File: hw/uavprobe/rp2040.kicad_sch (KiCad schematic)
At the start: 44 parts, among them IC1 UCLAMP3306P.TCT, SW1 Boot, U1 W25Q16JVSS, U2 NCP1117-5.0_SOT223, U3 RP2040, U4 TJA1051T-3, U5 TJA1051T-3, Y1 ABLS-12.000MHZ-B4-T

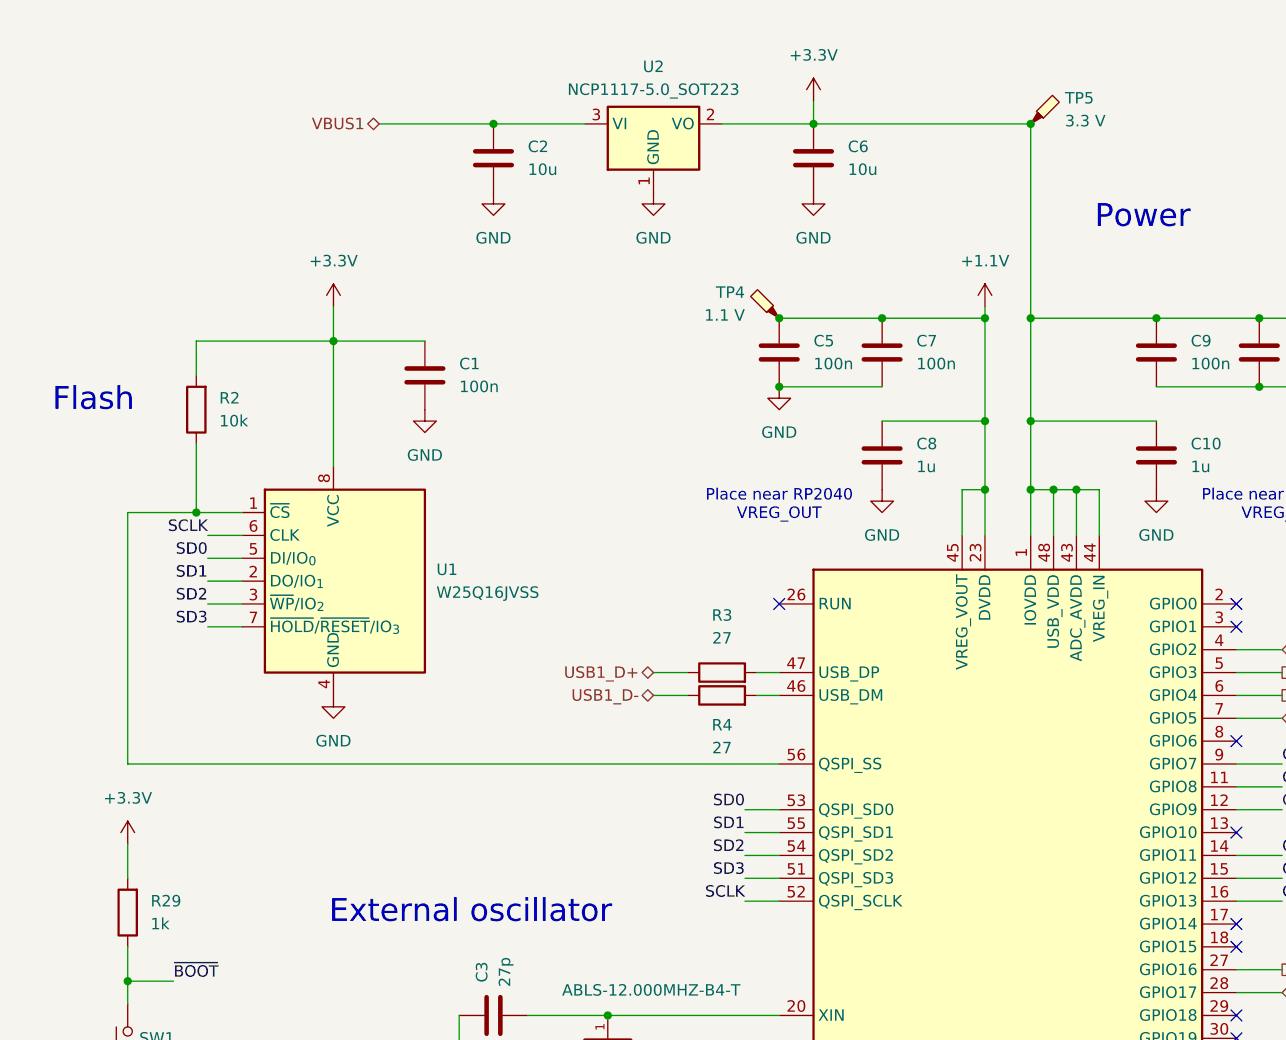
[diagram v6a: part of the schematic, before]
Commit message: Training layout
Lessons were learned, let's restart.
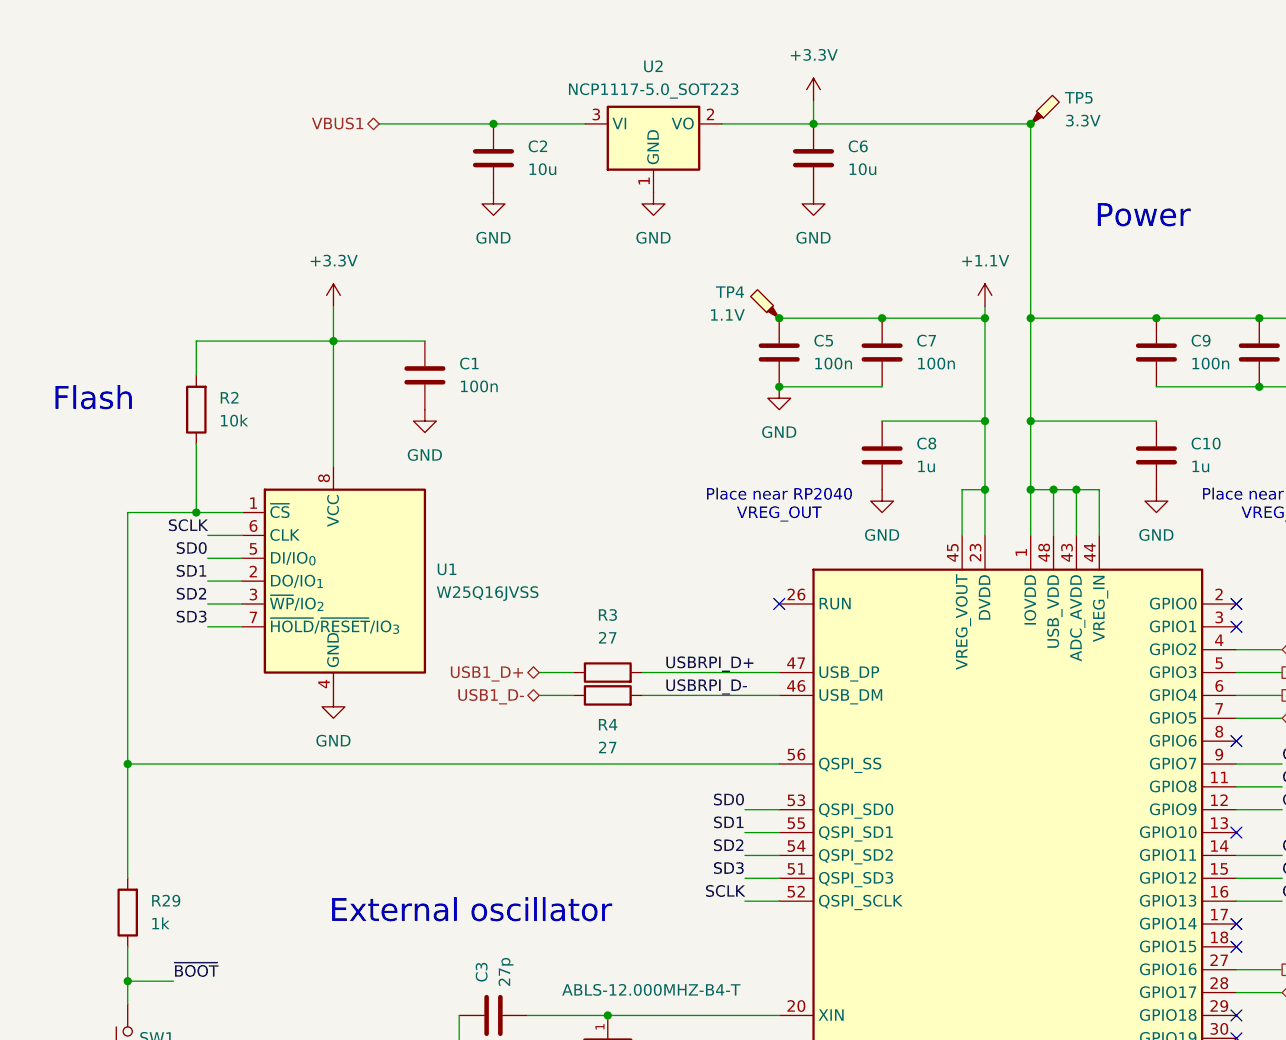
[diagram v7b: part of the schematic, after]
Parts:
- R3, R4: footprint Resistor_SMD:R_0402_1005Metric -> Resistor_SMD:R_0603_1608Metric
- TP4: value 1.1 V -> 1.1V
- TP5: value 3.3 V -> 3.3V
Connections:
- net +3.3V: no longer R29.2
- net USBRPI_D+: now reaches R3.2, U3.47 (USB_DP)
- net USBRPI_D-: now reaches R4.2, U3.46 (USB_DM)
- net at R2.1, U1.1 (~{CS}), U3.56 (QSPI_SS): now also R29.2
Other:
- moved on the sheet: R3, R4
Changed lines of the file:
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@@
 	)
 	(junction
+		(at 25.4 99.06)
+		(diameter 0)
+		(color 0 0 0 0)
+	)
+	(junction
 		(at 173.99 57.15)
 		(diameter 0)
@@
 	(wire
 		(pts
-			(xy 25.4 111.76) (xy 25.4 107.95)
-		)
-		(stroke
-			(width 0)
-			(type default)
-		)
-	)
-	(wire
-		(pts
-			(xy 95.25 88.9) (xy 97.79 88.9)
+			(xy 82.55 88.9) (xy 97.79 88.9)
 		)
 		(stroke
@@
 	(wire
 		(pts
-			(xy 95.25 91.44) (xy 97.79 91.44)
+			(xy 82.55 91.44) (xy 97.79 91.44)
 		)
 		(stroke
@@
 	(wire
 		(pts
+			(xy 25.4 111.76) (xy 25.4 99.06)
+		)
+		(stroke
+			(width 0)
+			(type default)
+		)
+	)
+	(wire
+		(pts
 			(xy 246.38 139.7) (xy 251.46 139.7)
 		)
@@
 	(wire
 		(pts
-			(xy 83.82 88.9) (xy 87.63 88.9)
+			(xy 71.12 88.9) (xy 74.93 88.9)
 		)
 		(stroke
@@
 	(wire
 		(pts
-			(xy 83.82 91.44) (xy 87.63 91.44)
+			(xy 71.12 91.44) (xy 74.93 91.44)
 		)
 		(stroke
@@
 		)
 	)
+	(label "USBRPI_D-"
+		(at 85.09 91.44 0)
+		(effects
+			(font
+				(size 1.27 1.27)
+			)
+			(justify left bottom)
+		)
+	)
+	(label "USBRPI_D+"
+		(at 85.09 88.9 0)
+		(effects
+			(font
+				(size 1.27 1.27)
+			)
+			(justify left bottom)
+		)
+	)
 	(label "SCLK"
 		(at 34.29 73.66 180)
@@
 	(hierarchical_label "USB1_D+"
 		(shape bidirectional)
-		(at 83.82 88.9 180)
+		(at 71.12 88.9 180)
 		(effects
 			(font
@@
 	(hierarchical_label "USB1_D-"
 		(shape bidirectional)
-		(at 83.82 91.44 180)
+		(at 71.12 91.44 180)
 		(effects
 			(font
@@
 			)
 		)
-		(property "Value" "3.3 V"
+		(property "Value" "3.3V"
 			(at 129.54 27.6224 0)
 			(effects
@@
 	(symbol
 		(lib_id "Device:R")
-		(at 91.44 88.9 90)
+		(at 78.74 88.9 90)
 		(unit 1)
 		(exclude_from_sim no)
@@
 		(fields_autoplaced yes)
 		(property "Reference" "R3"
-			(at 91.44 82.55 90)
+			(at 78.74 82.55 90)
 			(effects
 				(font
@@
 		)
 		(property "Value" "27"
-			(at 91.44 85.09 90)
+			(at 78.74 85.09 90)
 			(effects
 				(font
@@
 			)
 		)
-		(property "Footprint" "Resistor_SMD:R_0402_1005Metric"
-			(at 91.44 90.678 90)
+		(property "Footprint" "Resistor_SMD:R_0603_1608Metric"
+			(at 78.74 90.678 90)
 			(effects
 				(font
@@
 		)
 		(property "Datasheet" "~"
-			(at 91.44 88.9 0)
+			(at 78.74 88.9 0)
 			(effects
 				(font
@@
 		)
 		(property "Description" "Resistor"
-			(at 91.44 88.9 0)
+			(at 78.74 88.9 0)
 			(effects
 				(font
@@
 		)
 		(property "MP" ""
-			(at 91.44 88.9 90)
+			(at 78.74 88.9 90)
 			(effects
 				(font
@@
 		)
 		(property "Manufacturer_Part_Number" ""
-			(at 91.44 88.9 90)
+			(at 78.74 88.9 90)
 			(effects
 				(font
@@
 	(symbol
 		(lib_id "Device:R")
-		(at 91.44 91.44 90)
+		(at 78.74 91.44 90)
 		(unit 1)
 		(exclude_from_sim no)
@@
 		(dnp no)
 		(property "Reference" "R4"
-			(at 91.44 94.742 90)
+			(at 78.74 94.742 90)
 			(effects
 				(font
@@
 		)
 		(property "Value" "27"
-			(at 91.44 97.282 90)
+			(at 78.74 97.282 90)
 			(effects
 				(font
@@
 			)
 		)
-		(property "Footprint" "Resistor_SMD:R_0402_1005Metric"
-			(at 91.44 93.218 90)
+		(property "Footprint" "Resistor_SMD:R_0603_1608Metric"
+			(at 78.74 93.218 90)
 			(effects
 				(font
@@
 		)
 		(property "Datasheet" "~"
-			(at 91.44 91.44 0)
+			(at 78.74 91.44 0)
 			(effects
 				(font
@@
 		)
 		(property "Description" "Resistor"
-			(at 91.44 91.44 0)
+			(at 78.74 91.44 0)
 			(effects
 				(font
@@
 		)
 		(property "MP" ""
-			(at 91.44 91.44 90)
+			(at 78.74 91.44 90)
 			(effects
 				(font
@@
 		)
 		(property "Manufacturer_Part_Number" ""
-			(at 91.44 91.44 90)
+			(at 78.74 91.44 90)
 			(effects
 				(font
@@
 	)
 	(symbol
-		(lib_id "power:+3.3V")
-		(at 25.4 107.95 0)
-		(unit 1)
-		(exclude_from_sim no)
-		(in_bom yes)
-		(on_board yes)
-		(dnp no)
-		(fields_autoplaced yes)
-		(property "Reference" "#PWR062"
-			(at 25.4 111.76 0)
-			(effects
-				(font
-					(size 1.27 1.27)
-				)
-				(hide yes)
-			)
-		)
-		(property "Value" "+3.3V"
-			(at 25.4 102.87 0)
-			(effects
-				(font
-					(size 1.27 1.27)
-				)
-			)
-		)
-		(property "Footprint" ""
-			(at 25.4 107.95 0)
-			(effects
-				(font
-					(size 1.27 1.27)
-				)
-				(hide yes)
-			)
-		)
-		(property "Datasheet" ""
-			(at 25.4 107.95 0)
-			(effects
-				(font
-					(size 1.27 1.27)
-				)
-				(hide yes)
-			)
-		)
-		(property "Description" "Power symbol creates a global label with name \"+3.3V\""
-			(at 25.4 107.95 0)
-			(effects
-				(font
-					(size 1.27 1.27)
-				)
-				(hide yes)
-			)
-		)
-		(pin "1"
-		)
-		(instances
-			(project "uavprobe"
-				(path "/e4efab0a-eb38-47b4-a7c8-7fdbedea4819/b637890e-36cc-449d-9355-32fb577ea192"
-					(reference "#PWR062")
-					(unit 1)
-				)
-			)
-		)
-	)
-	(symbol
 		(lib_id "power:GND")
 		(at 214.63 149.86 0)
@@
 			)
 		)
-		(property "Value" "1.1 V"
+		(property "Value" "1.1V"
 			(at 93.98 49.2124 0)
 			(effects

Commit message: Layout revision 1
Pre-DRC
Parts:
- R4: footprint Resistor_SMD:R_0603_1608Metric -> Resistor_SMD:R_0402_1005Metric
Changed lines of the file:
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@@
 			)
 		)
-		(property "Footprint" "Resistor_SMD:R_0603_1608Metric"
+		(property "Footprint" "Resistor_SMD:R_0402_1005Metric"
 			(at 78.74 93.218 90)
 			(effects
